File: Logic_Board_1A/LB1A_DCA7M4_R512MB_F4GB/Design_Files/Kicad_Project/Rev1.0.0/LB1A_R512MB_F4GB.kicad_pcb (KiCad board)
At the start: 6 copper layers, 50 x 50 mm, 145 parts, among them U1 STM32MP157CAC3, U2 AS4C256M16D3LC-12BCN, U3 S40FC004C1B2C00000, U4 STPMIC1BPQR, U5 DF40C-70DP-0.4V(51), U6 DF40C-70DP-0.4V(51), U7 DF40C-70DP-0.4V(51), X1 32.768kHz, X2 24MHz

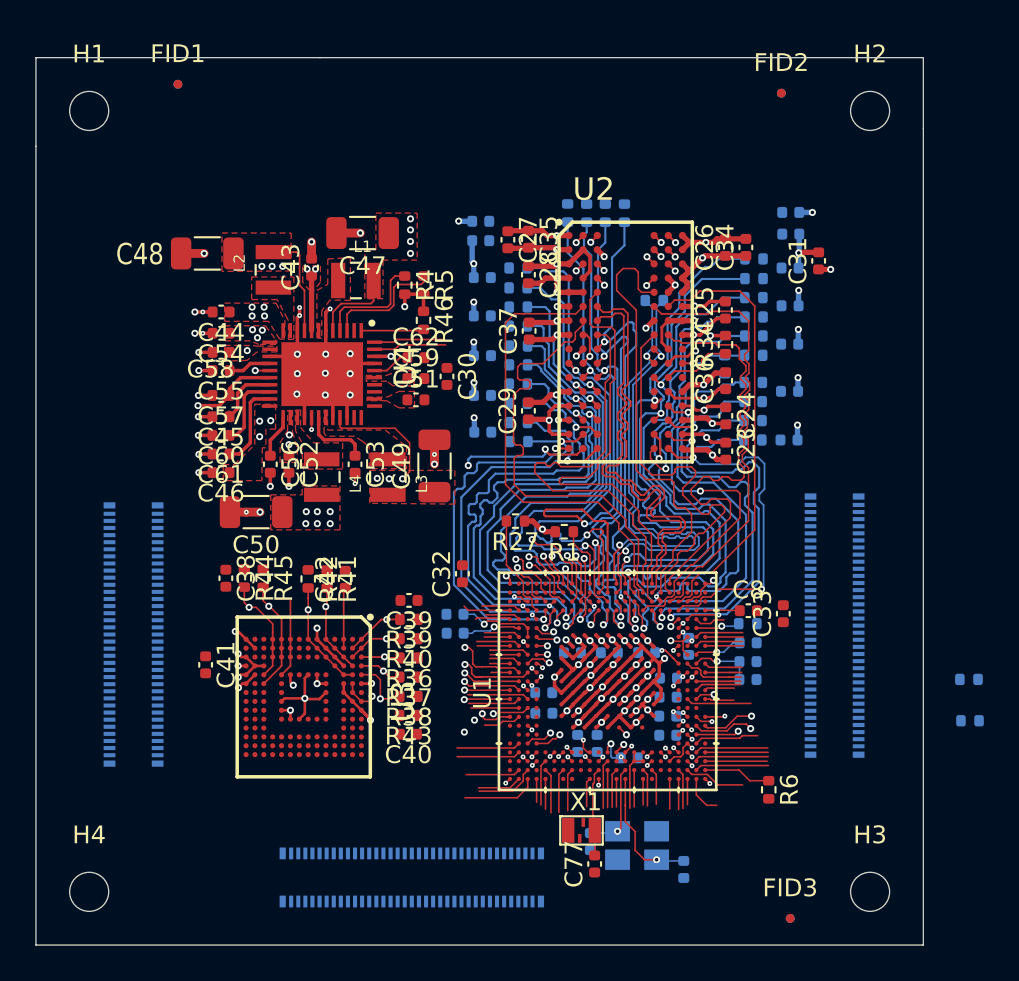
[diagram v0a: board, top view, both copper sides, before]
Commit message: PCB completed upto connectors
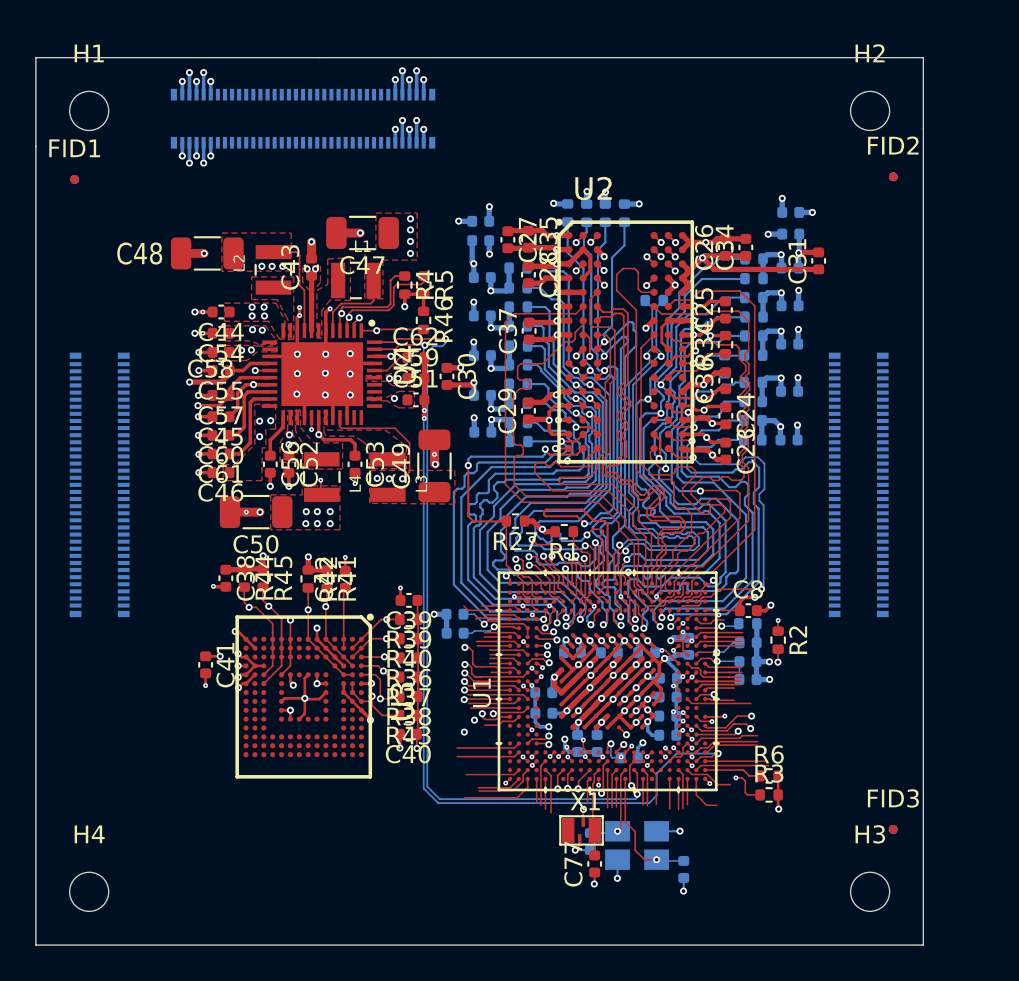
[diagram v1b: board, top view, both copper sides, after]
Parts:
- removed C32, C33: 100nF, Capacitor_SMD:C_0402_1005Metric
- R2, R3: moved to F.Cu
- moved U6 43.2 mm to (130.1, 69.9)
- moved R3 12.1 mm to (156.3, 108.0)
- moved R2 11.0 mm to (156.8, 99.3), turned to 270 degrees
- moved U5 8.64 mm to (118.6, 90.6)
- moved U7 8.05 mm to (161.4, 90.6)
- moved FID1 7.91 mm to (117.2, 73.4)
- moved FID4 7.91 mm to (117.2, 73.4)
- moved FID2 7.87 mm to (163.3, 73.2)
- moved FID5 7.87 mm to (163.3, 73.2)
- moved FID3 7.66 mm to (163.3, 110.0)
- moved FID6 7.66 mm to (163.3, 110.0)
- moved R6 0.78 mm to (156.3, 107.0), turned to 0 degrees
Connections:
- U6 pad 1: Net-(U6-Pad1) -> GND
- U6 pad 10: Net-(U6-Pad10) -> 5V_VIN
- U6 pad 2: Net-(U6-Pad2) -> 5V_VIN
- U6 pad 3: Net-(U6-Pad3) -> GND
- U6 pad 4: Net-(U6-Pad4) -> 5V_VIN
- U6 pad 5: Net-(U6-Pad5) -> GND
- U6 pad 6: Net-(U6-Pad6) -> 5V_VIN
- U6 pad 61: Net-(U6-Pad61) -> GND
- U6 pad 62: Net-(U6-Pad62) -> GND
- U6 pad 63: Net-(U6-Pad63) -> GND
- U6 pad 64: Net-(U6-Pad64) -> GND
- U6 pad 65: Net-(U6-Pad65) -> GND
- U6 pad 66: Net-(U6-Pad66) -> GND
- U6 pad 67: Net-(U6-Pad67) -> GND
- U6 pad 68: Net-(U6-Pad68) -> GND
- U6 pad 69: Net-(U6-Pad69) -> GND
- U6 pad 7: Net-(U6-Pad7) -> GND
- U6 pad 70: Net-(U6-Pad70) -> GND
- U6 pad 8: Net-(U6-Pad8) -> 5V_VIN
- U6 pad 9: Net-(U6-Pad9) -> GND
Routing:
- net PMIC_VREF_DDR: track 10.3 -> 68.7 mm, vias 2 -> 4
- net GND: track 148.2 -> 200.3 mm, vias 104 -> 138
- net NRST: track 10.7 -> 59.9 mm, vias 0 -> 3
- net PMIC_WAKEUP: track 0.00 -> 46.7 mm, vias 0 -> 2
- net PMIC_LDO4_VDD_USB: track 1.91 -> 44.7 mm, vias 1 -> 3
- net I2C4_SDA: track 9.31 -> 50.5 mm, vias 0 -> 2
- net PA0_WKUP: track 8.31 -> 48.3 mm, vias 0 -> 2
- net I2C4_SCL: track 8.82 -> 47.4 mm, vias 0 -> 2
- net POWER_ON: track 6.09 -> 43.8 mm, vias 0 -> 2
- net PMIC_LDO3_VTT_DDR: track 0.00 -> 35.8 mm, vias 1 -> 20
- net PMIC_VOUT1_VDD_CORE: track 20.8 -> 56.5 mm
- net PMIC_VOUT3_VDD: track 31.5 -> 62.5 mm, vias 18 -> 27
- net MPU_VDDA_1V8_REG: track 5.04 -> 15.0 mm
- net PMIC_VOUT2_VDD_DDR: track 46.3 -> 55.6 mm, vias 23 -> 22
- net I2C1_SDA: track 0.38 -> 7.38 mm, vias 1 -> 2
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- added copper zone on Signal_Layer_2.Cu, net 5V_VIN
- added copper zone on Signal_Layer_1.Cu, net GND
- added copper zone on Signal_Layer_3.Cu, net PMIC_LDO3_VTT_DDR
- added copper zone on Signal_Layer_3.Cu, net PMIC_VOUT1_VDD_CORE
- added copper zone on Signal_Layer_4.Cu, net PMIC_VOUT2_VDD_DDR
- added copper zone on Signal_Layer_3.Cu, net PMIC_VOUT3_VDD

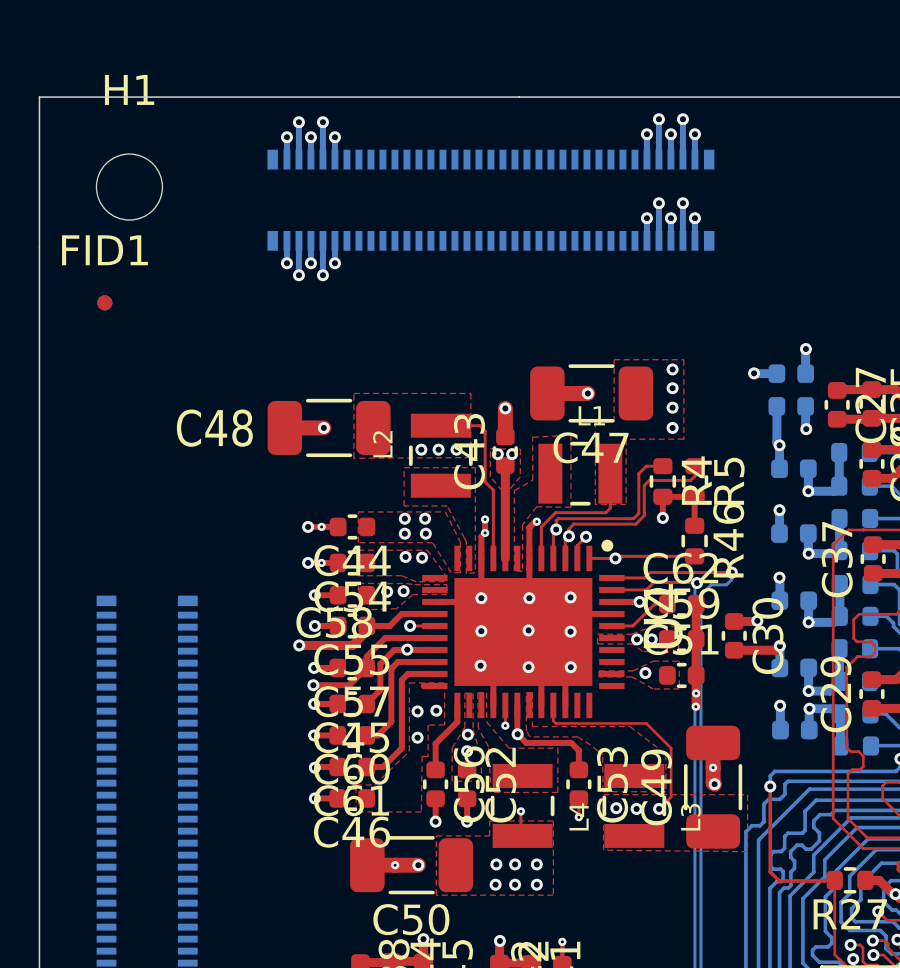
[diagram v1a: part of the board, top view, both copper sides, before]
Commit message: completed power connector
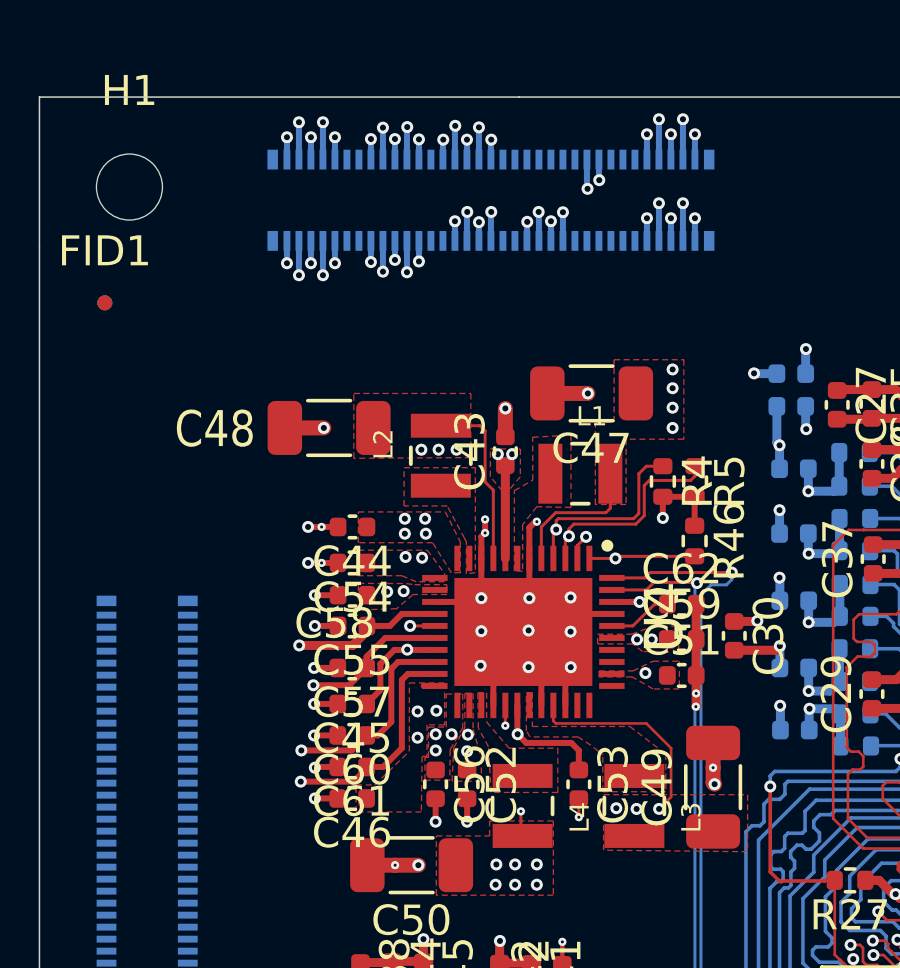
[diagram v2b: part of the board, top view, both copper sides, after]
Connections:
- U6 pad 15: Net-(U6-Pad15) -> PMIC_VOUT3_VDD
- U6 pad 16: Net-(U6-Pad16) -> PMIC_LDO1_1V8
- U6 pad 17: Net-(U6-Pad17) -> PMIC_VOUT3_VDD
- U6 pad 18: Net-(U6-Pad18) -> PMIC_LDO1_1V8
- U6 pad 19: Net-(U6-Pad19) -> PMIC_VOUT3_VDD
- U6 pad 20: Net-(U6-Pad20) -> PMIC_LDO1_1V8
- U6 pad 21: Net-(U6-Pad21) -> PMIC_VOUT3_VDD
- U6 pad 22: Net-(U6-Pad22) -> PMIC_LDO1_1V8
- U6 pad 23: Net-(U6-Pad23) -> PMIC_VOUT3_VDD
- U6 pad 24: Net-(U6-Pad24) -> PMIC_LDO1_1V8
- U6 pad 27: Net-(U6-Pad27) -> PMIC_VOUT4_3V3
- U6 pad 29: Net-(U6-Pad29) -> PMIC_VOUT4_3V3
- U6 pad 30: Net-(U6-Pad30) -> PMIC_LDO2_2V9
- U6 pad 31: Net-(U6-Pad31) -> PMIC_VOUT4_3V3
- U6 pad 32: Net-(U6-Pad32) -> PMIC_LDO2_2V9
- U6 pad 33: Net-(U6-Pad33) -> PMIC_VOUT4_3V3
- U6 pad 34: Net-(U6-Pad34) -> PMIC_LDO2_2V9
- U6 pad 35: Net-(U6-Pad35) -> PMIC_VOUT4_3V3
- U6 pad 36: Net-(U6-Pad36) -> PMIC_LDO2_2V9
- U6 pad 42: Net-(U6-Pad42) -> PMIC_LDO6_1V0
- U6 pad 44: Net-(U6-Pad44) -> PMIC_LDO6_1V0
- U6 pad 46: Net-(U6-Pad46) -> PMIC_LDO6_1V0
- U6 pad 48: Net-(U6-Pad48) -> PMIC_LDO6_1V0
- U6 pad 51: Net-(U6-Pad51) -> PMIC_LDO5
- U6 pad 53: Net-(U6-Pad53) -> PMIC_LDO5
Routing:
- net PMIC_LDO5: track 4.33 -> 46.4 mm, vias 0 -> 3
- net PMIC_LDO6_1V0: track 4.89 -> 41.1 mm, vias 0 -> 5
- net PMIC_LDO1_1V8: track 2.45 -> 30.8 mm, vias 0 -> 8
- net PMIC_LDO2_2V9: track 4.82 -> 32.5 mm, vias 1 -> 5
- net PMIC_VOUT4_3V3: track 4.60 -> 8.80 mm, vias 8 -> 13
- net PMIC_VOUT3_VDD: track 62.5 -> 66.7 mm, vias 27 -> 32
- added copper zone on F.Cu, net PMIC_LDO1_1V8
- added copper zone on Signal_Layer_3.Cu, net PMIC_LDO1_1V8
- added copper zone on Signal_Layer_2.Cu, net PMIC_LDO2_2V9
- added copper zone on Signal_Layer_2.Cu, net PMIC_LDO6_1V0
- added copper zone on Signal_Layer_4.Cu, net PMIC_VOUT4_3V3

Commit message: working on connectors
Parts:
- moved R2 0.70 mm to (157.3, 98.8), turned to 0 degrees
- moved C77 0.57 mm to (145.9, 111.8), turned to 0 degrees
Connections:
- U5 pad 40: Net-(U5-Pad40) -> LCD_G3
- U5 pad 42: Net-(U5-Pad42) -> LCD_B4
- U5 pad 44: Net-(U5-Pad44) -> LCD_B3
- U5 pad 46: Net-(U5-Pad46) -> STLINK_UART4_RX
- U5 pad 48: Net-(U5-Pad48) -> STLINK_UART4_TX
- U5 pad 50: Net-(U5-Pad50) -> I2S2_WS
- U5 pad 52: Net-(U5-Pad52) -> LCD_G1
- U5 pad 54: Net-(U5-Pad54) -> DSI_D0_P
- U5 pad 56: Net-(U5-Pad56) -> DSI_CKN
- U5 pad 58: Net-(U5-Pad58) -> DSI_CKP
- U5 pad 60: Net-(U5-Pad60) -> DSI_D1_N
- U5 pad 62: Net-(U5-Pad62) -> DSI_D1_P
- U5 pad 64: Net-(U5-Pad64) -> JTDO_TRACESWO
- U5 pad 66: Net-(U5-Pad66) -> NJRST
- U5 pad 68: Net-(U5-Pad68) -> JTDI
- U5 pad 70: Net-(U5-Pad70) -> JTCK_SWCLK
- U7 pad 14: Net-(U7-Pad14) -> LCD_R1
- U7 pad 16: Net-(U7-Pad16) -> ETH_RX_CLK
- U7 pad 18: Net-(U7-Pad18) -> ETH_NRST
- U7 pad 20: Net-(U7-Pad20) -> ETH_GTX_CLK
- U7 pad 22: Net-(U7-Pad22) -> ETH_MDIO
- U7 pad 24: Net-(U7-Pad24) -> U_LED_2
- U7 pad 25: Net-(U7-Pad25) -> STUSB1600_IRQOUTn
- U7 pad 26: Net-(U7-Pad26) -> LCD_R0
- U7 pad 27: Net-(U7-Pad27) -> LCD_HSYNC
- U7 pad 28: Net-(U7-Pad28) -> ETH_MDC
- U7 pad 29: Net-(U7-Pad29) -> U_BUTTON_2
- U7 pad 30: Net-(U7-Pad30) -> LCD_G0
- U7 pad 31: Net-(U7-Pad31) -> ANA0
- U7 pad 32: Net-(U7-Pad32) -> LCD_R5
- U7 pad 33: Net-(U7-Pad33) -> ANA1
- U7 pad 34: Net-(U7-Pad34) -> ETH_CLK125
- U7 pad 35: Net-(U7-Pad35) -> LCD_B5
- U7 pad 36: Net-(U7-Pad36) -> ETH_RXD2
- U7 pad 37: Net-(U7-Pad37) -> HDMI_INT
- U7 pad 38: Net-(U7-Pad38) -> ETH_RXD1
- U7 pad 39: Net-(U7-Pad39) -> ETH_TXD3
- U7 pad 40: Net-(U7-Pad40) -> USART1_TX
- U7 pad 41: Net-(U7-Pad41) -> ETH_TXD2
- U7 pad 42: Net-(U7-Pad42) -> ETH_RXD0
- U7 pad 43: Net-(U7-Pad43) -> ETH_TXD1
- U7 pad 44: Net-(U7-Pad44) -> ETH_RX_DV
- U7 pad 45: Net-(U7-Pad45) -> ETH_TX_EN
- U7 pad 46: Net-(U7-Pad46) -> ETH_MDINT
- U7 pad 47: Net-(U7-Pad47) -> ETH_TXD0
- U7 pad 48: Net-(U7-Pad48) -> ETH_CLK
- U7 pad 49: Net-(U7-Pad49) -> I2C1_SDA
- U7 pad 51: Net-(U7-Pad51) -> ETH_RXD3
- U7 pad 54: Net-(U7-Pad54) -> LCD_DE
- U7 pad 55: Net-(U7-Pad55) -> USART1_RX
- U7 pad 56: Net-(U7-Pad56) -> SPI5_MISO
- U7 pad 57: Net-(U7-Pad57) -> USB_DP2
- U7 pad 58: Net-(U7-Pad58) -> LCD_B2
- U7 pad 59: Net-(U7-Pad59) -> USB_DM2
- U7 pad 60: Net-(U7-Pad60) -> SPI5_SCK
- U7 pad 61: Net-(U7-Pad61) -> USB_DP1
- U7 pad 62: Net-(U7-Pad62) -> SPI5_MOSI
- U7 pad 63: Net-(U7-Pad63) -> USB_DM1
- U7 pad 65: Net-(U7-Pad65) -> HDMI_NRST
- U7 pad 66: Net-(U7-Pad66) -> SPI5_NSS
- U7 pad 67: Net-(U7-Pad67) -> I2C1_SCL
- U7 pad 68: Net-(U7-Pad68) -> LCD_CLK
- U7 pad 69: Net-(U7-Pad69) -> DSI_BL_CTRL
- U7 pad 70: Net-(U7-Pad70) -> USART1_RTS
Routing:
- net LCD_G1: track 3.47 -> 45.1 mm, vias 0 -> 1
- net STLINK_UART4_TX: track 2.71 -> 43.3 mm, vias 0 -> 1
- net LCD_G3: track 0.36 -> 40.8 mm, vias 1 -> 3
- net I2S2_WS: track 2.93 -> 42.0 mm, vias 0 -> 1
- net STLINK_UART4_RX: track 2.12 -> 40.8 mm, vias 0 -> 1
- net LCD_B3: track 3.59 -> 41.0 mm, vias 0 -> 1
- net LCD_B4: track 3.58 -> 39.0 mm, vias 0 -> 1
- net STUSB1600_IRQOUTn: track 0.50 -> 35.0 mm, vias 1 -> 3
- net DSI_D1_N: track 1.46 -> 34.3 mm, vias 0 -> 1
- net JTDO_TRACESWO: track 1.99 -> 34.7 mm, vias 0 -> 1
- net JTDI: track 2.69 -> 35.1 mm, vias 0 -> 1
- net JTCK_SWCLK: track 2.19 -> 34.5 mm, vias 0 -> 1
- net ANA1: track 0.38 -> 32.5 mm, vias 1 -> 3
- net NJRST: track 1.99 -> 34.1 mm, vias 0 -> 1
- net DSI_CKN: track 1.85 -> 33.8 mm, vias 0 -> 1
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
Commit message: working on connectors
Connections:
- U5 pad 35: Net-(U5-Pad35) -> BOOT1
- U5 pad 37: Net-(U5-Pad37) -> BOOT0
- U5 pad 38: Net-(U5-Pad38) -> LCD_R7
- U5 pad 39: Net-(U5-Pad39) -> U_BUTTON_1
- U5 pad 41: Net-(U5-Pad41) -> BOOT2
- U5 pad 43: Net-(U5-Pad43) -> LCD_B7
- U5 pad 45: Net-(U5-Pad45) -> LCD_B1
- U5 pad 47: Net-(U5-Pad47) -> LCD_VSYNC
- U5 pad 49: Net-(U5-Pad49) -> USART1_CTS
- U5 pad 51: Net-(U5-Pad51) -> LCD_B6
- U5 pad 53: Net-(U5-Pad53) -> LCD_B0
- U5 pad 55: Net-(U5-Pad55) -> LCD_G7
- U5 pad 57: Net-(U5-Pad57) -> I2S2_SDO
- U5 pad 59: Net-(U5-Pad59) -> LCD_G6
- U5 pad 61: Net-(U5-Pad61) -> LCD_G2
- U5 pad 63: Net-(U5-Pad63) -> LCD_G5
- U5 pad 65: Net-(U5-Pad65) -> LCD_R4
- U5 pad 67: Net-(U5-Pad67) -> LCD_G4
- U5 pad 69: Net-(U5-Pad69) -> LCD_R6
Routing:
- net LCD_B6: track 24.0 -> 56.3 mm, vias 2 -> 3
- net LCD_R6: track 16.5 -> 48.6 mm, vias 0 -> 1
- net BOOT2: track 27.3 -> 59.0 mm, vias 0 -> 1
- net LCD_VSYNC: track 27.3 -> 59.0 mm, vias 2 -> 3
- net LCD_B7: track 27.6 -> 59.0 mm, vias 2 -> 3
- net USART1_CTS: track 24.3 -> 55.5 mm, vias 2 -> 3
- net BOOT0: track 27.3 -> 58.4 mm, vias 0 -> 1
- net LCD_R4: track 17.8 -> 48.7 mm, vias 0 -> 1
- net LCD_B1: track 28.8 -> 59.6 mm, vias 2 -> 3
- net LCD_G6: track 20.1 -> 50.9 mm, vias 0 -> 1
- net BOOT1: track 30.6 -> 61.3 mm, vias 2 -> 3
- net U_BUTTON_1: track 27.7 -> 58.2 mm, vias 0 -> 1
- net LCD_G2: track 18.5 -> 48.7 mm, vias 0 -> 1
- net LCD_G7: track 20.5 -> 50.5 mm, vias 0 -> 1
- net LCD_G4: track 16.9 -> 46.7 mm, vias 0 -> 1
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
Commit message: Fully Routed
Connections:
- U5 pad 10: Net-(U5-Pad10) -> LCD_R2
- U5 pad 12: Net-(U5-Pad12) -> LCD_R3
- U5 pad 14: Net-(U5-Pad14) -> DSI_LCD_INT
- U5 pad 16: Net-(U5-Pad16) -> DSI_D0_N
- U5 pad 18: Net-(U5-Pad18) -> DSI_TE
- U5 pad 20: Net-(U5-Pad20) -> SDMMC1_CMD
- U5 pad 22: Net-(U5-Pad22) -> SDMMC1_CK
- U5 pad 24: Net-(U5-Pad24) -> I2S2_CK
- U5 pad 25: Net-(U5-Pad25) -> U_LED_1
- U5 pad 26: Net-(U5-Pad26) -> SDMMC1_D2
- U5 pad 27: Net-(U5-Pad27) -> nPONKEY
- U5 pad 28: Net-(U5-Pad28) -> SDMMC1_D3
- U5 pad 29: Net-(U5-Pad29) -> I2C4_SCL
- U5 pad 30: Net-(U5-Pad30) -> SDMMC1_D1
- U5 pad 31: Net-(U5-Pad31) -> I2C4_SDA
- U5 pad 32: Net-(U5-Pad32) -> SDMMC1_D0
- U5 pad 33: Net-(U5-Pad33) -> NRST
- U5 pad 34: Net-(U5-Pad34) -> JTMS_SWDIO
- U5 pad 36: Net-(U5-Pad36) -> DSI_RESET
- U7 pad 53: Net-(U7-Pad53) -> HDMI_CEC
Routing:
- net U_LED_1: track 0.34 -> 57.4 mm, vias 1 -> 3
- net SDMMC1_D1: track 1.22 -> 30.9 mm, vias 1 -> 2
- net SDMMC1_D2: track 0.62 -> 30.2 mm, vias 1 -> 2
- net SDMMC1_D0: track 1.13 -> 30.5 mm, vias 1 -> 2
- net SDMMC1_D3: track 0.61 -> 29.9 mm, vias 1 -> 2
- net SDMMC1_CMD: track 0.37 -> 28.9 mm, vias 1 -> 2
- net SDMMC1_CK: track 0.36 -> 28.8 mm, vias 1 -> 2
- net NRST: track 59.9 -> 88.2 mm
- net LCD_R2: track 4.36 -> 32.6 mm, vias 1 -> 2
- net LCD_R3: track 4.93 -> 33.0 mm, vias 1 -> 2
- net I2C4_SDA: track 50.5 -> 77.0 mm
- net I2S2_CK: track 3.76 -> 29.7 mm, vias 1 -> 2
- net I2C4_SCL: track 47.4 -> 73.3 mm
- net DSI_RESET: track 3.39 -> 28.8 mm, vias 1 -> 2
- net JTMS_SWDIO: track 2.48 -> 27.6 mm, vias 1 -> 2
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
